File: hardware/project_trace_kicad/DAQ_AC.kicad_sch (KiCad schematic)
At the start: 33 parts, among them U301 ADS1602, U303 THS4521ID, U304 LM358

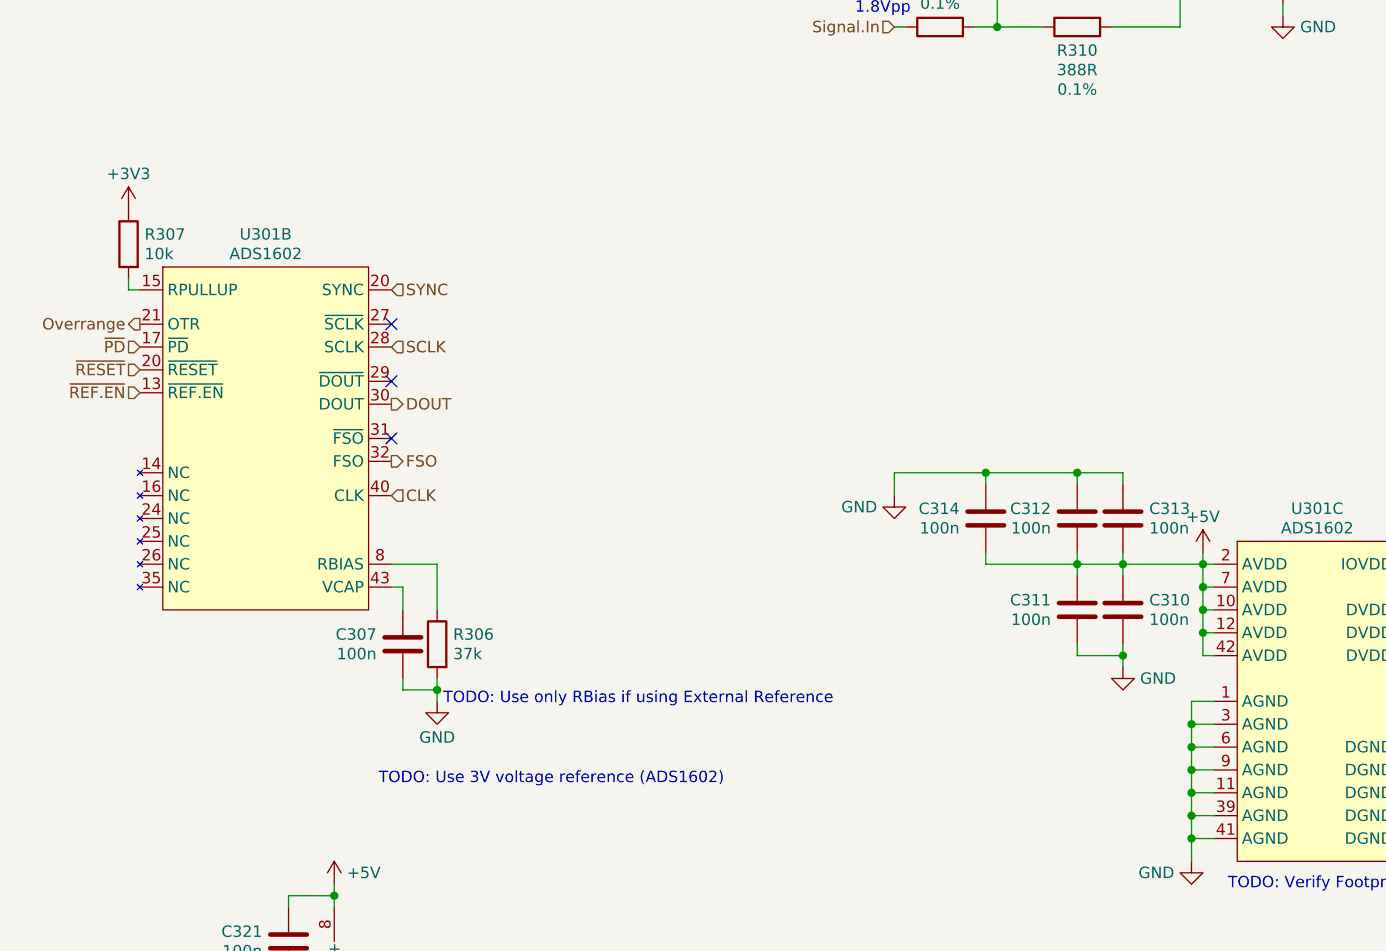
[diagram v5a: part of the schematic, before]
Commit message: Add Pull-Up Network to Input
(Sync up laptop)
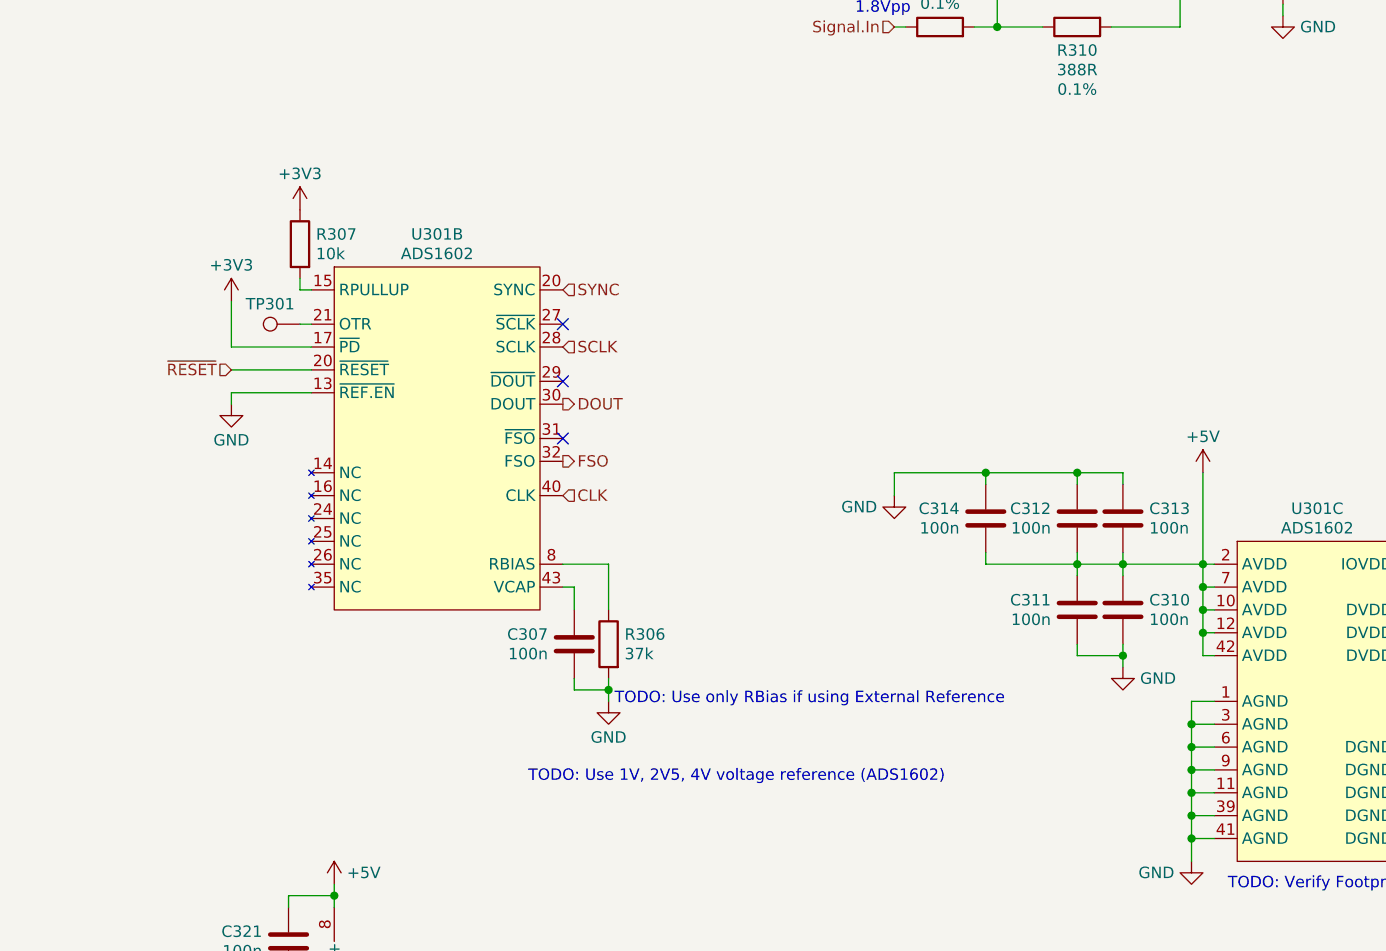
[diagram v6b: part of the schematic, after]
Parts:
- added TP301: TestPoint, TestPoint:TestPoint_Pad_1.5x1.5mm, symbol Connector:TestPoint
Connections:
- net ~{PD} is gone; now on net +3V3: U301.17 (~{PD})
- net ~{REF.EN} is gone; now on net GND: U301.13 (~{REF.EN})
- net Overrange: no longer names the net of U301.21 (OTR)
- net Overrange: now also TP301.1
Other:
- note added: "TODO: Use 1V, 2V5, 4V voltage reference (ADS1602)"
- note removed: "TODO: Use 3V voltage reference (ADS1602)"
- moved on the sheet: C307, R306, R307, U301B

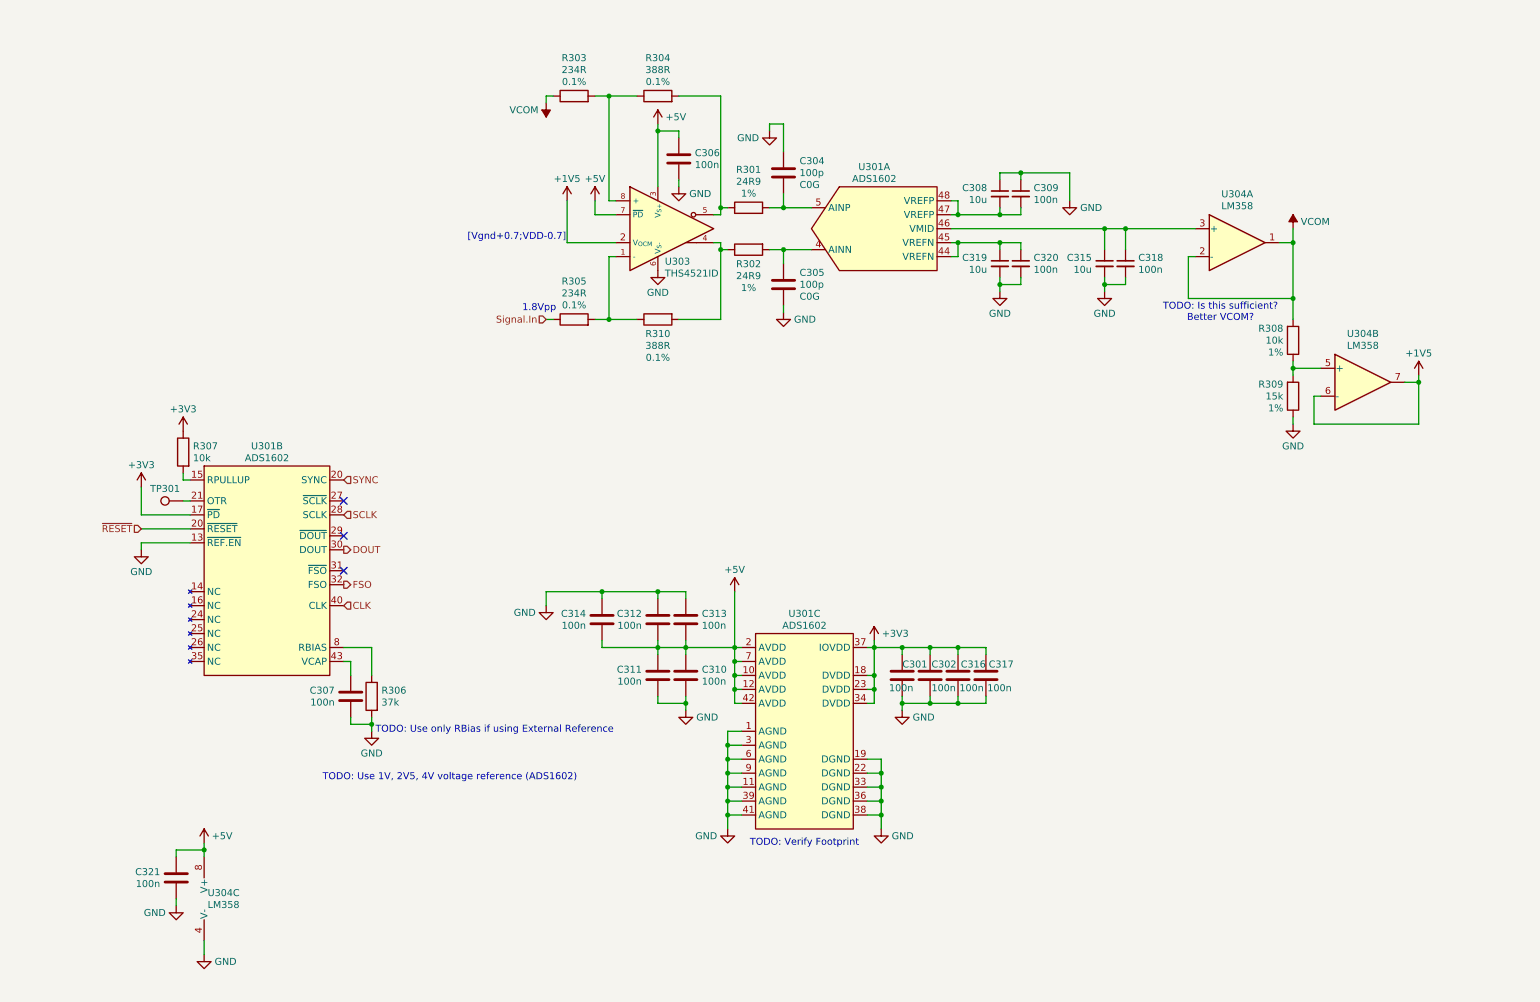
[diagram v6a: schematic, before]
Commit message: Change designators, Improve Input Circuit
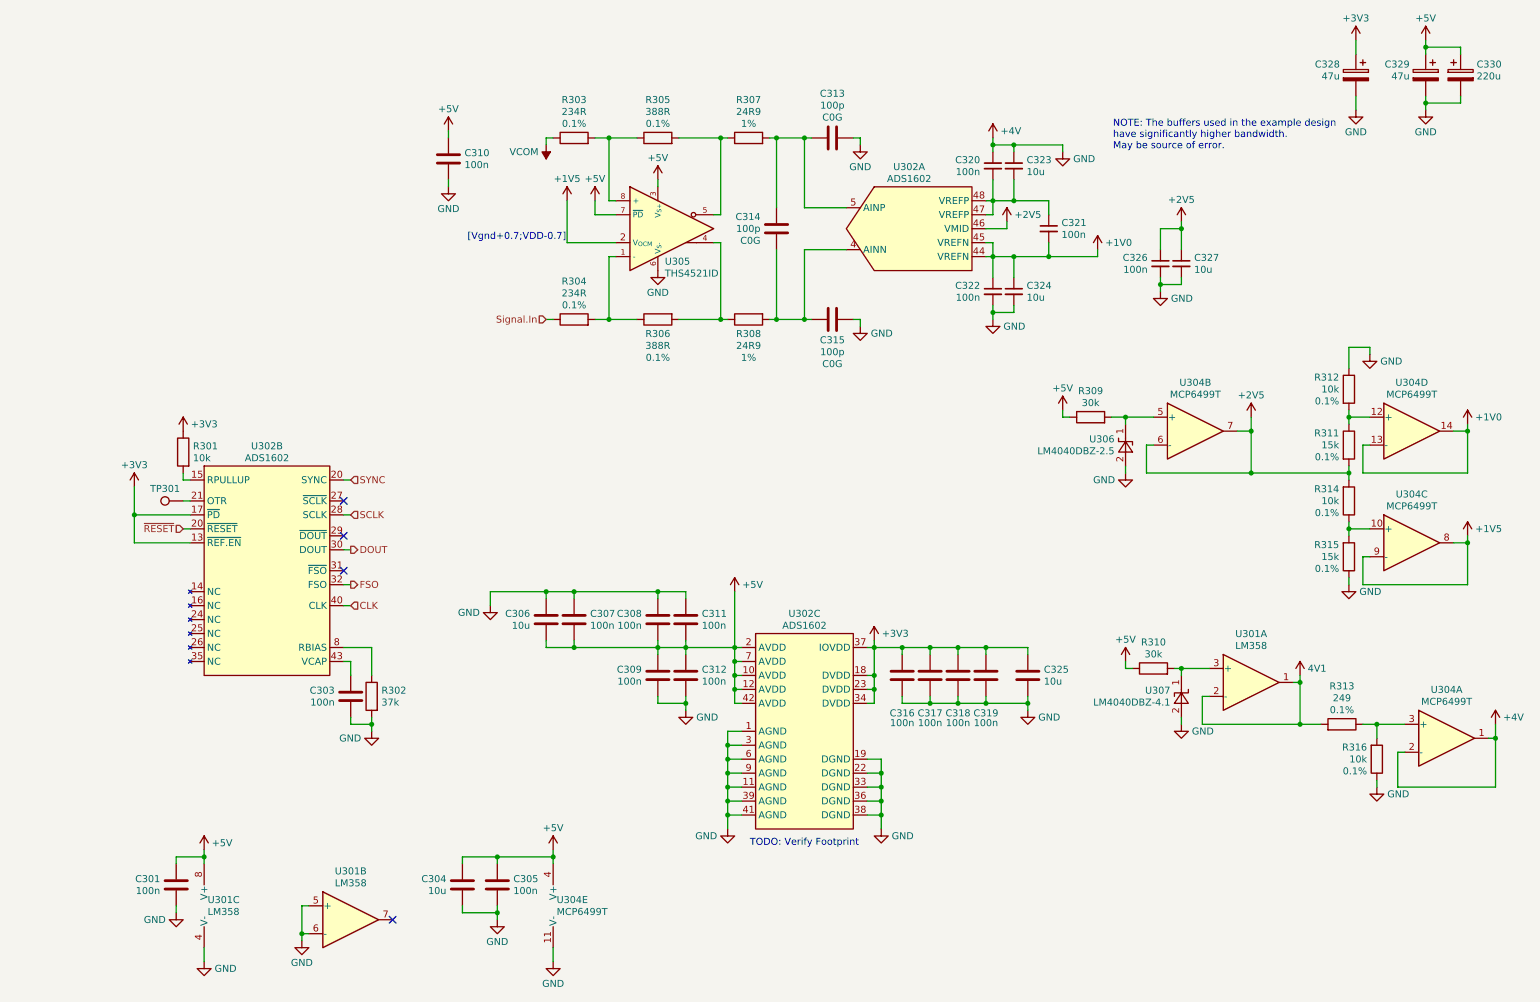
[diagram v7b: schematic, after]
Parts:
- removed unit 2 of U304
- removed unit 1 of U304
- added C304, C306, C325: 10u, Capacitor_SMD:C_0603_1608Metric_Pad1.08x0.95mm_HandSolder, symbol Device:C
- added C305: 100n, Capacitor_SMD:C_0603_1608Metric_Pad1.08x0.95mm_HandSolder, symbol Device:C
- added C314: 100p, Capacitor_SMD:C_0603_1608Metric_Pad1.08x0.95mm_HandSolder, symbol Device:C
- added C321: 100n, Capacitor_SMD:C_0603_1608Metric_Pad1.08x0.95mm_HandSolder, symbol Device:C_Small
- added C328, C329: 47u, symbol Device:C_Polarized
- added C330: 220u, symbol Device:C_Polarized
- added R309, R310: 30k, Resistor_SMD:R_0603_1608Metric_Pad0.98x0.95mm_HandSolder, symbol Device:R
- added R311: 15k, Resistor_SMD:R_0603_1608Metric_Pad0.98x0.95mm_HandSolder, symbol Device:R
- added R312, R316: 10k, Resistor_SMD:R_0603_1608Metric_Pad0.98x0.95mm_HandSolder, symbol Device:R
- added R313: 249, Resistor_SMD:R_0603_1608Metric_Pad0.98x0.95mm_HandSolder, symbol Device:R
- added unit 2 of U301
- added unit 1 of U301
- added U304: MCP6499T, ProjectTraceFootprints:SOIC-14_3.9x8.7mm_P1.27mm_Handsolder, symbol ProjectTraceSymbols:MCP6499T
- added U306: LM4040DBZ-2.5, Package_TO_SOT_SMD:SOT-23_Handsoldering, symbol Reference_Voltage:LM4040DBZ-2.5
- added U307: LM4040DBZ-4.1, Package_TO_SOT_SMD:SOT-23_Handsoldering, symbol Reference_Voltage:LM4040DBZ-4.1
- R314: renamed from R308; DigikeyPN (none) -> YAG1236CT-ND; Extra 1% -> 0.1%
- R315: renamed from R309; DigikeyPN (none) -> YAG1538CT-ND; Extra 1% -> 0.1%
- renumbered C321 to C301, C307 to C303, C314 to C307, C312 to C308, C311 to C309, C306 to C310, C313 to C311, C310 to C312, C304 to C313, C305 to C315, C301 to C316, C302 to C317, C316 to C318, C317 to C319, C309 to C320, C320 to C322, C308 to C323, C319 to C324, C318 to C326, C315 to C327, R307 to R301, R306 to R302, R305 to R304, R304 to R305, R310 to R306, R301 to R307, R302 to R308, U304 to U301, U301 to U302, U303 to U305
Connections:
- net +1V5: now also U304.8, U304.9 (-)
- net +3V3: now also U302.13 (~{REF.EN}), C325.2, C328.1
- net +5V: now also C304.2, C305.2, C306.1, C329.1, C330.1, R309.1, R310.1, U304.4 (V+)
- net VCOM: no longer R314.2
- net at R314.1, R315.2: now also U304.10 (+)
- net +2V5: now reaches C326.1, C327.1, U302.46 (VMID)
- net +2V5: now also R314.2, R311.2, U304.6 (-), U304.7
- net at R307.2, U302.5 (AINP): now also C313.1, C314.1; no longer C313.2
- net at C315.1, R308.2, U302.4 (AINN): now also C314.2
- net at C320.2, C323.2, U302.47 (VREFP)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: now also C321.1
- net +1V0: now reaches C322.1, C324.1, U302.44 (VREFN), U302.45 (VREFN)
- net +1V0: now also C321.2, U304.13 (-), U304.14
- net GND renamed +4V
- net +4V: now also C313.2, C304.1, C305.1, C306.2, C325.1, C328.2, C329.2, C330.2, R312.1, R316.1, U301.5 (+), U301.6 (-), U304.1, U304.11 (V-), U304.2 (-), U306.2 (A), U307.2 (A); no longer C313.1, U302.13 (~{REF.EN})
- new net: R309.2, U304.5 (+), U306.1 (K)
- new net: R311.1, R312.2, U304.12 (+)
- new net: R310.2, U301.3 (+), U307.1 (K)
- new net: R313.1, R316.2, U304.3 (+)
- new net 4V1: R313.2, U301.1, U301.2 (-)
- no-connect marks 3 -> 4
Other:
- note added: "NOTE: The buffers used in the example design have significantly higher bandwidth. May be source of error."
- note removed: "1.8Vpp"
- note removed: "TODO: Is this sufficient? Better VCOM?"
- note removed: "TODO: Use 1V, 2V5, 4V voltage reference (ADS1602)"
- note removed: "TODO: Use only RBias if using External Reference"
- moved on the sheet: C301, C307, C310, C313, C315, C320, C322, C323, C324, C326, C327, R303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

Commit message: Improve Inputs, Source Parts, Add Credits
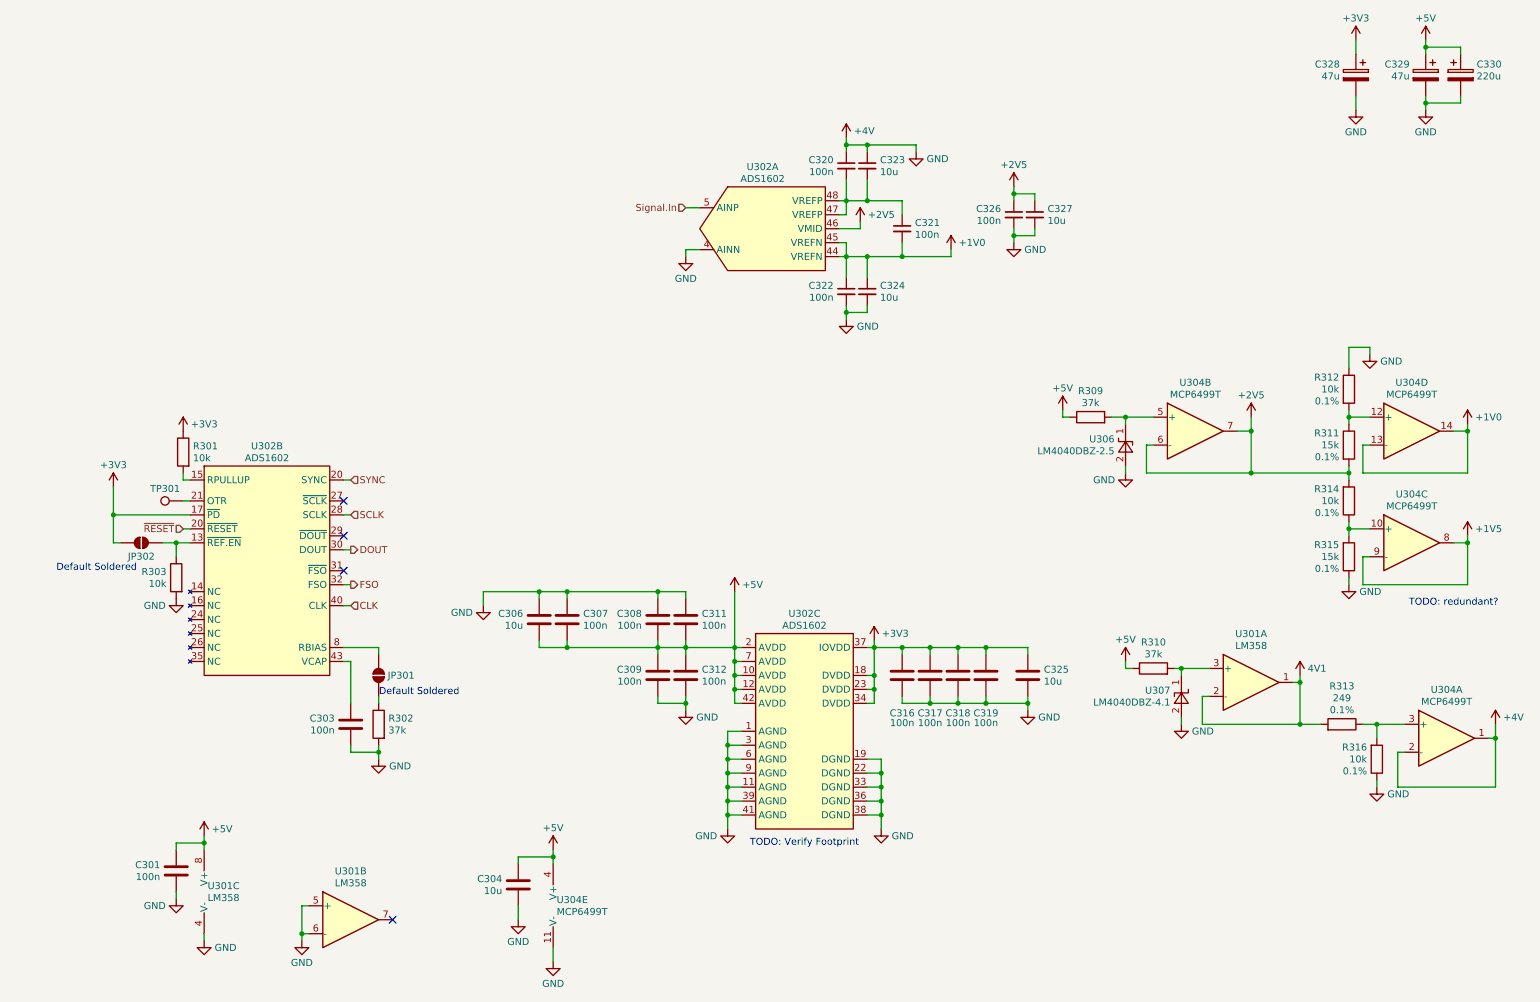
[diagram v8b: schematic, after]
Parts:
- removed C305, C310: 100n, Capacitor_SMD:C_0603_1608Metric_Pad1.08x0.95mm_HandSolder, symbol Device:C
- removed C313, C314, C315: 100p, Capacitor_SMD:C_0603_1608Metric_Pad1.08x0.95mm_HandSolder, symbol Device:C
- removed R304: 234R, Resistor_SMD:R_0603_1608Metric_Pad0.98x0.95mm_HandSolder, symbol Device:R
- removed R305, R306: 388R, Resistor_SMD:R_0603_1608Metric_Pad0.98x0.95mm_HandSolder, symbol Device:R
- removed R307, R308: 24R9, Resistor_SMD:R_0603_1608Metric_Pad0.98x0.95mm_HandSolder, symbol Device:R
- removed U305: THS4521ID, Package_SO:SOIC-8_3.9x4.9mm_P1.27mm, symbol Amplifier_Difference:THS4521ID
- added JP301, JP302: SolderJumper_2_Open, symbol Jumper:SolderJumper_2_Open
- C301, C303, C307, C308, C309, C311, C312, C316, C317, C318, C319, C320, C321, C322, C326: DigikeyPN (none) -> 399-C0603C104K3RACTUCT-ND; Extra (none) -> 25V
- C304, C306, C323, C324, C325, C327: footprint Capacitor_SMD:C_0603_1608Metric_Pad1.08x0.95mm_HandSolder -> Capacitor_SMD:C_0805_2012Metric_Pad1.18x1.45mm_HandSolder; DigikeyPN (none) -> 490-10516-1-ND
- C328, C329, C330, TP301: DigikeyPN (none) -> N/A
- R301: DigikeyPN (none) -> YAG1236CT-ND
- R302: DigikeyPN (none) -> 2019-RN73R1JTTD3702F100CT-ND
- R303: value 234R -> 10k; DigikeyPN (none) -> YAG1236CT-ND; Extra 0.1% -> (none)
- R309, R310: value 30k -> 37k; DigikeyPN (none) -> 2019-RN73R1JTTD3702F100CT-ND
- R313: DigikeyPN (none) -> YAG1597CT-ND
- U306: DigikeyPN (none) -> LM4040B25FTADICT-ND
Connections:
- net +3V3: now also JP302.2 (B); no longer U302.13 (~{REF.EN})
- net +4V: now also R303.2, U302.4 (AINN)
- net Signal.In: now also U302.5 (AINP)
- net at R302.1: now also JP301.1 (A); no longer U302.8 (RBIAS)
- net VCOM: no longer names the net of R303.1
- net VCOM: now also U302.13 (~{REF.EN}), JP302.1 (A)
- new net: JP301.2 (B), U302.8 (RBIAS)
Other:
- note added: "Default Soldered"
- note added: "TODO: redundant?"
- note removed: "NOTE: The buffers used in the example design have significantly higher bandwidth. May be source of error."
- note removed: "[Vgnd+0.7;VDD-0.7]"
- title: (none) -> Multilloscope - ADC
- moved on the sheet: C301, C303, C304, C306, C307, C320, C321, C322, C323, C324, C326, C327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
